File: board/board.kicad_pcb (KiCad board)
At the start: 2 copper layers, 22 parts, among them U1 STM32F405RGTx, U2 MP2359, U3 MX25R3235FM2xx1, Y1 16MHz

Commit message: Updated board
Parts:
- added C13: 10u, Capacitor_SMD:C_0603_1608Metric, F.Cu at (83.8, 58.4)
- added C14: 10n, Capacitor_SMD:C_0603_1608Metric, F.Cu at (90.0, 45.9)
- added C15: 2u2, Capacitor_SMD:C_0603_1608Metric, F.Cu at (90.0, 48.4)
- added C16: 2u2, Capacitor_SMD:C_0603_1608Metric, F.Cu at (85.8, 53.1)
- added C17: 1u, Capacitor_SMD:C_0402_1005Metric, F.Cu at (93.3, 50.6)
- added C18: 10n, Capacitor_SMD:C_0402_1005Metric, F.Cu at (89.3, 55.7)
- added C19: 1u, Capacitor_SMD:C_0402_1005Metric, F.Cu at (77.5, 64.8)
- added C20: 100n, Capacitor_SMD:C_0402_1005Metric, F.Cu at (72.6, 74.0)
- added D1: D_Schottky_Small, Diode_SMD:D_0603_1608Metric, F.Cu at (75.8, 57.2)
- added D2: B5819W, Diode_SMD:D_0603_1608Metric, F.Cu at (85.2, 50.6)
- added D3: POW LED [Gr], LED_SMD:LED_0603_1608Metric, F.Cu at (116.8, 52.1)
- added F1: 300mA, Fuse:Fuse_1206_3216Metric, F.Cu at (76.6, 54.3)
- added FB1: 600 @ 100 MHz, Inductor_SMD:L_0603_1608Metric, F.Cu at (94.0, 45.9)
- added FB2: 600 @ 100 MHz, Inductor_SMD:L_0603_1608Metric, F.Cu at (79.8, 58.4)
- added H1: MountingHole, MountingHole:MountingHole_3.5mm_Pad_Via, F.Cu at (68.6, 94.0)
- added H2: MountingHole, MountingHole:MountingHole_3.5mm_Pad_Via, F.Cu at (121.9, 94.0)
- added H3: MountingHole, MountingHole:MountingHole_3.5mm_Pad_Via, F.Cu at (68.5, 125.7)
- added H4: MountingHole, MountingHole:MountingHole_3.5mm_Pad_Via, F.Cu at (121.9, 125.7)
- added J1: USB_B_Micro, Connector_USB:USB_Micro-B_Amphenol_10103594-0001LF_Horizontal, F.Cu at (78.5, 48.5)
- added J2: Molex Picoblade, Connector_Molex:Molex_PicoBlade_53047-0310_1x03_P1.25mm_Vertical, F.Cu at (68.6, 40.6)
- added L1: 10u, Inductor_SMD:L_0603_1608Metric, F.Cu at (85.8, 55.6)
- added Q1: AO3401A, Package_TO_SOT_SMD:SOT-23, F.Cu at (81.6, 54.9)
- added Q2: Find one, Package_TO_SOT_SMD:SOT-23, F.Cu at (73.4, 70.7)
- added R10: 15k, Resistor_SMD:R_0603_1608Metric, F.Cu at (89.8, 53.4)
- added R11: 270, Resistor_SMD:R_0603_1608Metric, F.Cu at (87.8, 58.1)
- added R12: 1.5k, Resistor_SMD:R_0603_1608Metric, F.Cu at (120.8, 52.0)
- added R13: 10k, Resistor_SMD:R_0402_1005Metric, F.Cu at (127.3, 51.8)
- added R2: 100, Resistor_SMD:R_0402_1005Metric, F.Cu at (80.4, 64.8)
- added R3: R_Small_US, Resistor_SMD:R_0402_1005Metric, F.Cu at (89.9, 41.1)
- added R7: 100k, Resistor_SMD:R_0603_1608Metric, F.Cu at (89.8, 50.9)
- added R8: 68k, Resistor_SMD:R_0603_1608Metric, F.Cu at (94.0, 48.4)
- added R9: 47k, Resistor_SMD:R_0603_1608Metric, F.Cu at (98.0, 45.9)
- added U4: USBLC6-2SC6, Package_TO_SOT_SMD:SOT-23-6, F.Cu at (85.6, 47.0)
- added U5: ELVH-100A-HANH-C-N2A5, Package_DIP:DIP-8_W7.62mm_LongPads, F.Cu at (61.5, 65.8)
- added U6: UCC2751x, Package_TO_SOT_SMD:SOT-23-5, F.Cu at (73.6, 66.1)
- moved U1 40.0 mm to (94.0, 108.0)
- moved C3 34.7 mm to (108.6, 81.1)
- moved C4 34.7 mm to (117.3, 72.5)
- moved C5 34.7 mm to (113.3, 75.0)
- moved C6 34.7 mm to (111.0, 77.1)
- moved C7 34.7 mm to (105.7, 81.1)
- moved R1 34.7 mm to (108.1, 77.1)
- moved R3 34.7 mm to (115.0, 70.2)
- moved C1 34.7 mm to (90.2, 80.0)
- moved C10 34.7 mm to (108.6, 79.1)
- moved C11 34.7 mm to (109.9, 72.3)
- moved C12 34.7 mm to (105.7, 79.1)
- moved C8 34.7 mm to (104.6, 76.8)
- moved C9 34.7 mm to (94.2, 80.0)
- moved R2 34.7 mm to (98.2, 80.0)
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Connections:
- U1 pad 33: Net-(U1-Pad33) -> SPI2_!CS
- U1 pad 34: Net-(U1-Pad34) -> SPI2_CLK
- U1 pad 35: Net-(U1-Pad35) -> SPI2_MISO
- U1 pad 36: Net-(U1-Pad36) -> SPI2_MOSI
- U1 pad 37: Net-(U1-Pad37) -> FLASH_!HOLD
- U1 pad 38: Net-(U1-Pad38) -> FLASH_!WP
- U1 pad 44: Net-(U1-Pad44) -> USB_D-
- U1 pad 45: Net-(U1-Pad45) -> USB_D+
- U2 pad 1: BUCK_IN -> BUCK_BST
- U2 pad 5: (no net) -> BUCK_IN
- Y1 pad 2: GND -> Net-(Y1-Pad2)
- Y1 pad 4: GND -> Net-(Y1-Pad2)
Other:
- board outline added: 63.5 x 41.9 mm

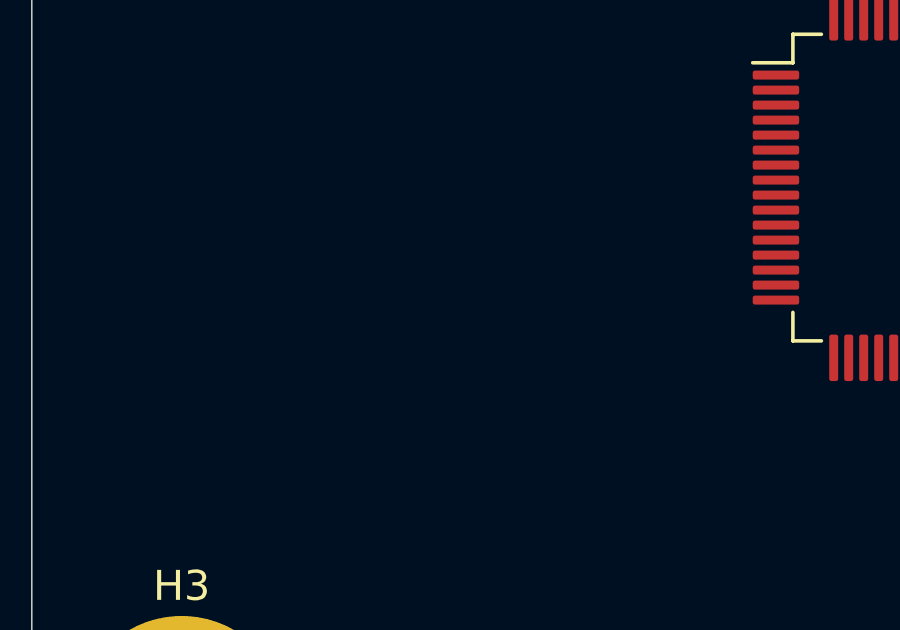
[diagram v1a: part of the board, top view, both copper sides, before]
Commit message: Rework on power supply and added pressure sensor
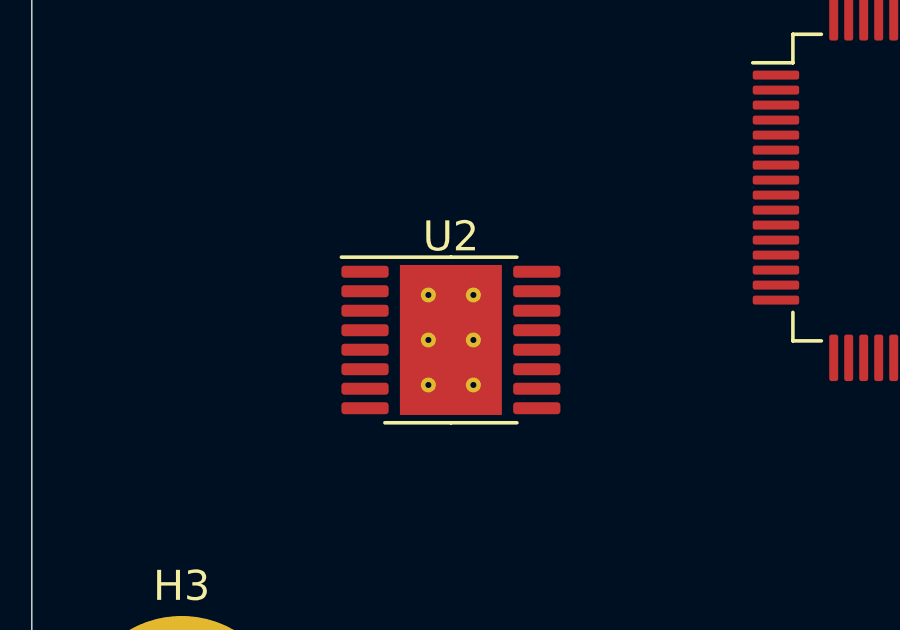
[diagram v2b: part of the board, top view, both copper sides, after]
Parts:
- added U2: TPS542941, Package_SO:HTSSOP-16-1EP_4.4x5mm_P0.65mm_EP3.4x5mm_Mask2.46x2.31mm_ThermalVias, F.Cu at (77.5, 113.0)

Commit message: Update
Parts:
- removed the C18 at (89.3, 55.7)
- removed the D1 at (75.8, 57.2)
- removed D2: B5819W, Diode_SMD:D_0603_1608Metric
- removed the J1 at (78.5, 48.5)
- removed the R11 at (87.8, 58.1)
- removed the R2 at (98.2, 80.0)
- removed the R3 at (89.9, 41.1)
- removed the R3 at (115.0, 70.2)
- removed the R7 at (89.8, 50.9)
- removed the U2 at (120.7, 64.8)
- removed the U4 at (85.6, 47.0)
- added C12: 10n, Capacitor_SMD:C_0402_1005Metric, F.Cu at (99.5, 70.1)
- added C19: 100n, Capacitor_SMD:C_0603_1608Metric, F.Cu at (140.1, 88.1)
- added C20: 10u, Capacitor_SMD:C_0603_1608Metric, F.Cu at (139.4, 100.3)
- added C21: 22u, Capacitor_SMD:C_0603_1608Metric, F.Cu at (136.0, 93.1)
- added J2: USB_B_Micro, Connector_USB:USB_Micro-B_Amphenol_10103594-0001LF_Horizontal, F.Cu at (171.9, 56.4)
- added J3: Conn_ARM_JTAG_SWD_10, Connector_PinHeader_1.27mm:PinHeader_2x05_P1.27mm_Vertical_SMD, F.Cu at (150.2, 62.2)
- added L2: 2u2, Inductor_SMD:L_0603_1608Metric, F.Cu at (139.4, 102.8)
- added R4: 124k, Resistor_SMD:R_0603_1608Metric, F.Cu at (151.6, 110.2)
- added R5: 22k1, Resistor_SMD:R_0603_1608Metric, F.Cu at (140.1, 93.1)
- added U6: USBLC6-2SC6, Package_TO_SOT_SMD:SOT-23-6, F.Cu at (180.9, 51.3)
- C11: value 2u2 -> 1u; footprint Capacitor_SMD:C_0603_1608Metric -> Capacitor_SMD:C_0402_1005Metric
- C13: value 10u -> 22u
- C14: value 10n -> 10u
- C15: value 2u2 -> 100n
- C16: value 2u2 -> 10u
- C17: footprint Capacitor_SMD:C_0402_1005Metric -> Capacitor_SMD:C_0603_1608Metric
- L1: value 10u -> 4u7
- R10: value 15k -> R_Small_US; footprint Resistor_SMD:R_0603_1608Metric -> Resistor_SMD:R_0402_1005Metric
- R8: value 68k -> 73k2
- R9: value 47k -> 22k1
- moved R9 85.6 mm to (151.6, 112.7)
- moved U2 83.9 mm to (139.0, 56.1)
- moved R8 72.8 mm to (139.4, 105.3)
- moved L1 64.5 mm to (140.1, 90.6)
- moved C14 62.4 mm to (136.0, 88.1)
- moved C15 62.3 mm to (140.1, 85.5)
- moved C13 58.8 mm to (136.0, 85.5)
- moved C17 58.5 mm to (136.0, 90.6)
- moved C5 46.7 mm to (98.4, 115.2)
- moved C4 43.3 mm to (81.5, 104.3)
- moved C3 43.0 mm to (90.8, 116.8)
- moved R3 41.5 mm to (143.4, 75.6)
- moved C6 41.1 mm to (98.4, 116.2)
- moved J1 40.4 mm to (55.6, 78.9)
- moved C8 37.5 mm to (99.7, 113.9)
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- renumbered C12 to C18, C3 to C2, C19 to C22, C20 to C23, C2 to C3, C5 to C4, C4 to C5, D3 to D1, J2 to J1, R13 to R11, R2 to R12, R12 to R2, R4 to R3, R5 to R6, R6 to R7, U5 to U4, U6 to U5
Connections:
- net Net-(U2-Pad11) renamed PG2_OUT
- net Net-(U2-Pad12) renamed EN2_IN
- net Net-(U2-Pad5) renamed EN1_IN
- net Net-(U2-Pad6) renamed PG1_OUT
- C1 pad 2: GND -> PGND1
- C10 pad 2: GND -> PGND1
- C11 pad 1: BUCK_IN -> +3.3VA
- C11 pad 2: GND -> PGND1
- C13 pad 1: BUCK_IN -> +5V
- C13 pad 2: GND -> PGND1
- C14 pad 1: BUCK_BST -> BUCK_IN
- C14 pad 2: BUCK_SW -> PGND1
- C15 pad 1: +3V3 -> VBST1
- C15 pad 2: GND -> SW1
- C16 pad 1: +3V3 -> BUCK_IN
- C16 pad 2: GND -> PGND1
- C17 pad 1: +3.3VA -> Net-(C17-Pad1)
- C17 pad 2: GND -> PGND1
- C18 pad 2: GND -> PGND1
- C2 pad 2: GND -> PGND1
- C22 pad 2: GND -> PGND1
- C23 pad 2: GND -> PGND1
- C3 pad 2: GND -> PGND1
- C4 pad 2: GND -> PGND1
- C5 pad 2: GND -> PGND1
- C6 pad 2: GND -> PGND1
- C7 pad 2: GND -> PGND1
- C8 pad 2: GND -> PGND1
- C9 pad 2: GND -> PGND1
- FB1 pad 1: BUCK_IN -> +3.3VA
- FB1 pad 2: Net-(F1-Pad1) -> +3V3
- FB2 pad 1: +3.3VA -> BUCK_IN
- FB2 pad 2: +3V3 -> Net-(F1-Pad1)
- L1 pad 1: BUCK_SW -> +5V
- L1 pad 2: +3V3 -> SW1
- Q1 pad 1: GND -> PGND1
- Q2 pad 2: GND -> PGND1
- R10 pad 2: BUCK_FB -> Net-(R10-Pad2)
- R2 pad 1: GND -> PGND1
- R8 pad 1: GND -> VFB2
- R8 pad 2: BUCK_EN -> +3V3
- R9 pad 1: BUCK_FB -> PGND1
- R9 pad 2: +3V3 -> VFB2
- U1 pad 12: GND -> PGND1
- U1 pad 18: GND -> PGND1
- U1 pad 63: GND -> PGND1
- U2 pad 10: Net-(U2-Pad10) -> VFB2
- U2 pad 13: Net-(U2-Pad13) -> PGND1
- U2 pad 14: Net-(U2-Pad14) -> SW2
- U2 pad 15: Net-(U2-Pad15) -> VBST2
- U2 pad 16: Net-(U2-Pad16) -> BUCK_IN
- U2 pad 2: Net-(U2-Pad2) -> VBST1
- U2 pad 3: Net-(U2-Pad3) -> SW1
- U2 pad 4: Net-(U2-Pad4) -> PGND1
- U2 pad 7: Net-(U2-Pad7) -> VFB1
- U2 pad 8: Net-(U2-Pad8) -> PGND1
- U2 pad 9: Net-(U2-Pad9) -> Net-(C17-Pad1)
- U3 pad 4: GND -> PGND1
- U4 pad 2: GND -> PGND1
- U5 pad 2: GND -> PGND1

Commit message: Generic update
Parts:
- added C24: 100n, Capacitor_SMD:C_0402_1005Metric, F.Cu at (138.1, 111.0)
- added C25: 100n, Capacitor_SMD:C_0402_1005Metric, F.Cu at (138.1, 113.0)
- added C26: 100n, Capacitor_SMD:C_0402_1005Metric, F.Cu at (138.1, 115.0)
- added C27: C_Small, Capacitor_SMD:C_0402_1005Metric, F.Cu at (106.1, 120.7)
- added J4: Conn_01x02_Male, Connector_PinHeader_2.54mm:PinHeader_1x02_P2.54mm_Vertical_SMD_Pin1Right, F.Cu at (108.6, 113.6)
- added J5: Conn_01x02_Male, Connector_PinHeader_2.54mm:PinHeader_1x02_P2.54mm_Vertical_SMD_Pin1Right, F.Cu at (116.5, 113.6)
- added R13: 220, Resistor_SMD:R_0603_1608Metric, F.Cu at (130.7, 113.8)
- added R14: 33, Resistor_SMD:R_0603_1608Metric, F.Cu at (134.7, 111.3)
- added R15: 10k, Resistor_SMD:R_0603_1608Metric, F.Cu at (134.7, 113.8)
- added R16: 100, Resistor_SMD:R_0603_1608Metric, F.Cu at (106.6, 118.4)
- added R17: 100, Resistor_SMD:R_0603_1608Metric, F.Cu at (110.6, 118.4)
- added R18: 100, Resistor_SMD:R_0603_1608Metric, F.Cu at (122.5, 111.3)
- added R19: 100, Resistor_SMD:R_0603_1608Metric, F.Cu at (114.6, 118.4)
- added R20: 100, Resistor_SMD:R_0603_1608Metric, F.Cu at (122.5, 113.8)
- added R7: 220, Resistor_SMD:R_0603_1608Metric, F.Cu at (130.7, 111.3)
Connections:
- J3 pad 1: Net-(J3-Pad1) -> +3V3
- J3 pad 10: Net-(J3-Pad10) -> SWD_!RESET
- J3 pad 3: Net-(J3-Pad3) -> PGND1
- J3 pad 5: Net-(J3-Pad3) -> PGND1
- U1 pad 34: SPI2_CLK -> Net-(R14-Pad2)
- U3 pad 2: Net-(R7-Pad2) -> SPI2_MISO

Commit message: Updated footprints
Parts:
- removed the R7 at (130.7, 111.3)
- removed the R7 at (130.9, 85.6)
- added C28: 100n, Capacitor_SMD:C_0402_1005Metric, F.Cu at (128.9, 75.6)
- added C29: 100n, Capacitor_SMD:C_0402_1005Metric, F.Cu at (123.1, 82.3)
- added C30: 100n, Capacitor_SMD:C_0402_1005Metric, F.Cu at (125.9, 75.6)
- added C31: 1u, Capacitor_SMD:C_0402_1005Metric, F.Cu at (122.9, 84.2)
- added C32: 100n, Capacitor_SMD:C_0402_1005Metric, F.Cu at (120.0, 84.9)
- added C33: 100n, Capacitor_SMD:C_0402_1005Metric, F.Cu at (130.3, 55.7)
- added D2: LED_RGB, LED_SMD:LED_RGB_1210, F.Cu at (93.3, 102.1)
- added Q3: Q_NMOS_GDS, Package_TO_SOT_SMD:SOT-23, F.Cu at (82.4, 52.0)
- added Q4: Q_NMOS_GDS, Package_TO_SOT_SMD:SOT-23, F.Cu at (75.6, 59.6)
- added Q5: Find one, Package_TO_SOT_SMD:SOT-23, F.Cu at (123.9, 79.0)
- added R21: 22, Resistor_SMD:R_0603_1608Metric, F.Cu at (113.4, 62.0)
- added R22: 22, Resistor_SMD:R_0603_1608Metric, F.Cu at (109.4, 62.0)
- added R23: 22, Resistor_SMD:R_0603_1608Metric, F.Cu at (130.9, 51.0)
- added R7: 220, Resistor_SMD:R_0603_1608Metric, F.Cu at (97.4, 56.0)
- C11: value 1u -> 100n
- C12: value 10n -> 100n
- C13: value 22u -> 100n; footprint Capacitor_SMD:C_0603_1608Metric -> Capacitor_SMD:C_0402_1005Metric
- C14: value 10u -> 1u; footprint Capacitor_SMD:C_0603_1608Metric -> Capacitor_SMD:C_0402_1005Metric
- C15: value 100n -> 22u
- C17: value 1u -> 10n; footprint Capacitor_SMD:C_0603_1608Metric -> Capacitor_SMD:C_0402_1005Metric
- C18: footprint Capacitor_SMD:C_0402_1005Metric -> Capacitor_SMD:C_0603_1608Metric
- C19: value 100n -> 10u
- C2, C4: value 12p -> 2u2; footprint Capacitor_SMD:C_0402_1005Metric -> Capacitor_SMD:C_0603_1608Metric
- C21: value 22u -> 1u
- C22: value 1u -> 100n; footprint Capacitor_SMD:C_0402_1005Metric -> Capacitor_SMD:C_0603_1608Metric
- C23: value 100n -> 10u; footprint Capacitor_SMD:C_0402_1005Metric -> Capacitor_SMD:C_0603_1608Metric
- C24: value 100n -> 22u; footprint Capacitor_SMD:C_0402_1005Metric -> Capacitor_SMD:C_0603_1608Metric
- C27: value C_Small -> 100n
- C5, C7: value 100n -> 12p
- C8, C9: value 2u2 -> 100n; footprint Capacitor_SMD:C_0603_1608Metric -> Capacitor_SMD:C_0402_1005Metric
- J2: value USB_B_Micro -> Conn_ARM_JTAG_SWD_10; footprint Connector_USB:USB_Micro-B_Amphenol_10103594-0001LF_Horizontal -> Connector_PinHeader_1.27mm:PinHeader_2x05_P1.27mm_Vertical_SMD
- J3: value Conn_ARM_JTAG_SWD_10 -> USB_B_Micro; footprint Connector_PinHeader_1.27mm:PinHeader_2x05_P1.27mm_Vertical_SMD -> Connector_USB:USB_Micro-B_Amphenol_10103594-0001LF_Horizontal
- J4: value Conn_01x02_Male -> Conn_01x04_Male; footprint Connector_PinHeader_2.54mm:PinHeader_1x02_P2.54mm_Vertical_SMD_Pin1Right -> Connector_PinHeader_2.54mm:PinHeader_1x04_P2.54mm_Vertical
- J5: value Conn_01x02_Male -> Screw_Terminal_01x02; footprint Connector_PinHeader_2.54mm:PinHeader_1x02_P2.54mm_Vertical_SMD_Pin1Right -> TerminalBlock_Phoenix:TerminalBlock_Phoenix_PT-1,5-2-5.0-H_1x02_P5.00mm_Horizontal
- Q2: value Find one -> Q_NMOS_GDS
- R1: value 47 -> 220; footprint Resistor_SMD:R_0402_1005Metric -> Resistor_SMD:R_0603_1608Metric
- R10: value R_Small_US -> 73k2; footprint Resistor_SMD:R_0402_1005Metric -> Resistor_SMD:R_0603_1608Metric
- R11: value 10k -> 22k1; footprint Resistor_SMD:R_0402_1005Metric -> Resistor_SMD:R_0603_1608Metric
- R12: value 100 -> 2k2; footprint Resistor_SMD:R_0402_1005Metric -> Resistor_SMD:R_0603_1608Metric
- R13: value 220 -> 10k; footprint Resistor_SMD:R_0603_1608Metric -> Resistor_SMD:R_0402_1005Metric
- R14: value 33 -> 10k
- R16: footprint Resistor_SMD:R_0603_1608Metric -> Resistor_SMD:R_0402_1005Metric
- R17: value 100 -> 10k
- R18, R19, R20: value 100 -> 22
- R2: value 1.5k -> 220
- R3: value 10k -> 47; footprint Resistor_SMD:R_0603_1608Metric -> Resistor_SMD:R_0402_1005Metric
- R4: value 124k -> 1.5k
- R5: value 22k1 -> 124k
- R6: value 10k -> 22k1
- R8: value 73k2 -> 120
- R9: value 22k1 -> 120
- U3: value MX25R3235FM2xx1 -> ELVH-100A-HANH-C-N2A5; footprint Package_SO:SOP-8_5.28x5.23mm_P1.27mm -> Package_DIP:DIP-8_W7.62mm_LongPads
- U4: value ELVH-100A-HANH-C-N2A5 -> UCC2751x; footprint Package_DIP:DIP-8_W7.62mm_LongPads -> Package_TO_SOT_SMD:SOT-23-5
- U5: value UCC2751x -> MX25R3235FM2xx1; footprint Package_TO_SOT_SMD:SOT-23-5 -> Package_SO:SOP-8_5.28x5.23mm_P1.27mm
- moved R9 81.5 mm to (81.8, 70.6)
- moved R4 79.5 mm to (93.4, 56.0)
- moved U6 77.1 mm to (105.0, 64.3)
- moved U2 76.6 mm to (63.3, 67.5)
- moved C24 76.2 mm to (91.1, 51.0)
- moved L1 70.3 mm to (75.4, 63.2)
- moved C20 70.1 mm to (85.4, 55.5)
- moved L2 67.4 mm to (93.4, 53.5)
- moved U4 67.3 mm to (126.9, 72.3)
- moved C21 66.4 mm to (73.8, 69.9)
- moved R8 65.6 mm to (93.4, 58.5)
- moved R5 63.0 mm to (83.4, 65.6)
- moved C19 62.6 mm to (83.8, 60.5)
- moved J4 61.6 mm to (104.9, 52.0)
- moved J1 61.0 mm to (116.7, 79.8)
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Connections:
- net Net-(U1-Pad10) renamed LCD_DB2
- net Net-(U1-Pad11) renamed LCD_DB3
- net Net-(U1-Pad15) renamed LCD_RS
- net Net-(U1-Pad16) renamed LCD_EN
- net Net-(U1-Pad17) renamed LCD_RW
- net Net-(U1-Pad30) renamed TIM2_CH4
- net Net-(U1-Pad41) renamed RCC_MCO1
- net Net-(U1-Pad8) renamed LCD_DB0
- net Net-(U1-Pad9) renamed LCD_DB1
- net PG1_OUT renamed Net-(U2-Pad6)
- net PG2_OUT renamed Net-(U2-Pad11)
- net SWD_TMS renamed SWO
- C11 pad 1: +3.3VA -> +3V3
- C12 pad 1: +3.3VA -> +3V3
- C13 pad 1: +5V -> +3V3
- C14 pad 1: BUCK_IN -> +3.3VA
- C15 pad 1: VBST1 -> +5V
- C15 pad 2: SW1 -> PGND1
- C17 pad 1: Net-(C17-Pad1) -> +3.3VA
- C18 pad 1: +3V3 -> VBST1
- C18 pad 2: PGND1 -> SW1
- C19 pad 1: VBST2 -> PGND1
- C19 pad 2: SW2 -> +3V3
- C2 pad 1: HSE_IN -> Net-(C2-Pad1)
- C21 pad 1: +3V3 -> Net-(C21-Pad1)
- C22 pad 1: +UCC_VDD -> VBST2
- C22 pad 2: PGND1 -> SW2
- C23 pad 1: +UCC_VDD -> BUCK_IN
- C25 pad 1: +3V3 -> +5V
- C26 pad 1: +3V3 -> +5V
- C27 pad 1: SWD_!RESET -> +5V
- C5 pad 1: +3V3 -> HSE_IN
- C7 pad 1: +3V3 -> Net-(C7-Pad1)
- C8 pad 1: Net-(C8-Pad1) -> +3V3
- C9 pad 1: Net-(C9-Pad1) -> +3V3
- J1 pad 1: Net-(J1-Pad1) -> TIM2_CH3
- J1 pad 2: Net-(J1-Pad2) -> PGND1
- J1 pad 3: Net-(J1-Pad3) -> +5V
- J2 pad 1: VBUS -> +3V3
- J2 pad 2: USB_CONN_D- -> Net-(J2-Pad2)
- J2 pad 3: USB_CONN_D+ -> PGND1
- J3 pad 1: +3V3 -> VBUS
- J3 pad 2: Net-(J3-Pad2) -> USB_CONN_D-
- J3 pad 3: PGND1 -> USB_CONN_D+
- J4 pad 1: Net-(J4-Pad1) -> +5V
- J5 pad 1: Net-(J5-Pad1) -> +UCC_VDD
- J5 pad 2: Net-(J5-Pad2) -> PGND1
- Q2 pad 1: Net-(Q2-Pad1) -> TIM4_CH1
- Q2 pad 2: PGND1 -> Net-(Q2-Pad2)
- Q2 pad 3: +UCC_VDD -> PGND1
- R1 pad 1: HSE_OUT -> USART3_TX
- R1 pad 2: Net-(C4-Pad1) -> Net-(R1-Pad2)
- R10 pad 1: Net-(R10-Pad1) -> VFB2
- R10 pad 2: Net-(R10-Pad2) -> +3V3
- R11 pad 1: UCC_EN -> PGND1
- R11 pad 2: +UCC_VDD -> VFB2
- R12 pad 1: Net-(Q2-Pad1) -> TIM2_CH3
- R12 pad 2: UCC_OUT -> +5V
- R13 pad 1: USART1_RX -> UCC_EN
- R13 pad 2: Net-(R13-Pad2) -> +UCC_VDD
- R14 pad 1: SPI2_CLK -> +3V3
- R14 pad 2: Net-(R14-Pad2) -> FLASH_!HOLD
- R15 pad 1: SPI2_MISO -> +3V3
- R15 pad 2: PGND1 -> FLASH_!WP
- R16 pad 1: SWD_TCK -> Net-(Q5-Pad1)
- R16 pad 2: Net-(J3-Pad4) -> UCC_OUT
- R17 pad 1: SWD_TDI -> SPI2_MISO
- R17 pad 2: Net-(J3-Pad8) -> PGND1
- R18 pad 1: SWD_TDO -> Net-(J2-Pad10)
- R18 pad 2: Net-(J3-Pad6) -> NRST
- R19 pad 1: SWD_!RESET -> SWDCLK
- R19 pad 2: +3V3 -> Net-(J2-Pad4)
- R2 pad 1: PGND1 -> USART3_RX
- R2 pad 2: Net-(D1-Pad1) -> Net-(R2-Pad2)
- R20 pad 2: Net-(J3-Pad2) -> Net-(J2-Pad6)
- R3 pad 1: +3V3 -> HSE_OUT
- R3 pad 2: FLASH_!HOLD -> Net-(C7-Pad1)
- R4 pad 1: VFB1 -> PGND1
- R4 pad 2: +5V -> Net-(D1-Pad1)
- R5 pad 1: PGND1 -> VFB1
- R5 pad 2: VFB1 -> +5V
- R6 pad 1: +3V3 -> PGND1
- R6 pad 2: FLASH_!WP -> VFB1
- R8 pad 1: VFB2 -> Net-(Q3-Pad2)
- R8 pad 2: +3V3 -> Net-(D2-Pad2)
- R9 pad 1: PGND1 -> Net-(Q4-Pad2)
- R9 pad 2: VFB2 -> Net-(D2-Pad3)
- U1 pad 20: Net-(U1-Pad20) -> SPI1_!CS
- U1 pad 21: Net-(U1-Pad21) -> SPI1_CLK
- U1 pad 22: Net-(U1-Pad22) -> SPI1_MISO
- U1 pad 23: Net-(U1-Pad23) -> SPI1_MOSI
- U1 pad 29: Net-(U1-Pad29) -> TIM2_CH3
- U1 pad 31: Net-(C8-Pad1) -> Net-(C2-Pad1)
- U1 pad 34: Net-(R14-Pad2) -> SPI2_CLK
- U1 pad 37: FLASH_!HOLD -> FLASH_!WP
- U1 pad 38: FLASH_!WP -> FLASH_!HOLD
- U1 pad 47: Net-(C9-Pad1) -> Net-(C4-Pad1)
- U1 pad 51: Net-(U1-Pad51) -> Net-(R1-Pad2)
- U1 pad 52: Net-(U1-Pad52) -> Net-(R2-Pad2)
- U1 pad 58: Net-(U1-Pad58) -> TIM4_CH1
- U1 pad 59: Net-(U1-Pad59) -> TIM4_CH2
- U1 pad 61: Net-(U1-Pad61) -> TIM4_CH3
- U2 pad 9: Net-(C17-Pad1) -> Net-(C21-Pad1)
- U3 pad 1: SPI2_!CS -> +5V
- U3 pad 2: SPI2_MISO -> PGND1
- U3 pad 3: FLASH_!WP -> Net-(U3-Pad3)
- U3 pad 4: PGND1 -> SPI1_MISO
- U3 pad 5: SPI2_MOSI -> SPI1_CLK
- U3 pad 6: SPI2_CLK -> SPI1_!CS
- U3 pad 7: FLASH_!HOLD -> Net-(U3-Pad7)
- U3 pad 8: +3V3 -> SPI1_MOSI
- U4 pad 1: ELVH_VDD -> UCC_EN
- U4 pad 3: Net-(U4-Pad3) -> UCC_IN
- U4 pad 4: SPI3_MISO -> UCC_OUT
- U4 pad 5: SPI3_SCLK -> +UCC_VDD
- U5 pad 1: UCC_EN -> SPI2_!CS
- U5 pad 2: PGND1 -> SPI2_MISO
- U5 pad 3: UCC_IN -> FLASH_!WP
- U5 pad 4: UCC_OUT -> PGND1
- U5 pad 5: +UCC_VDD -> SPI2_MOSI
- Y1 pad 3: Net-(C4-Pad1) -> Net-(C7-Pad1)
